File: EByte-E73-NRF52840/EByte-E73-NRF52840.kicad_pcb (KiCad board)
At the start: 2 copper layers, 19.1 x 52.1 mm, 32 parts, among them J1 USB_B_Micro, J2 SWD Header, J3 Conn_01x02, Q1 TP0610T, SW1 DFU, SW2 FRST, U1 ProMicro, U2 E73-2G4M08S1C, U3 AP2112K-3.3, U4 TP4054ST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

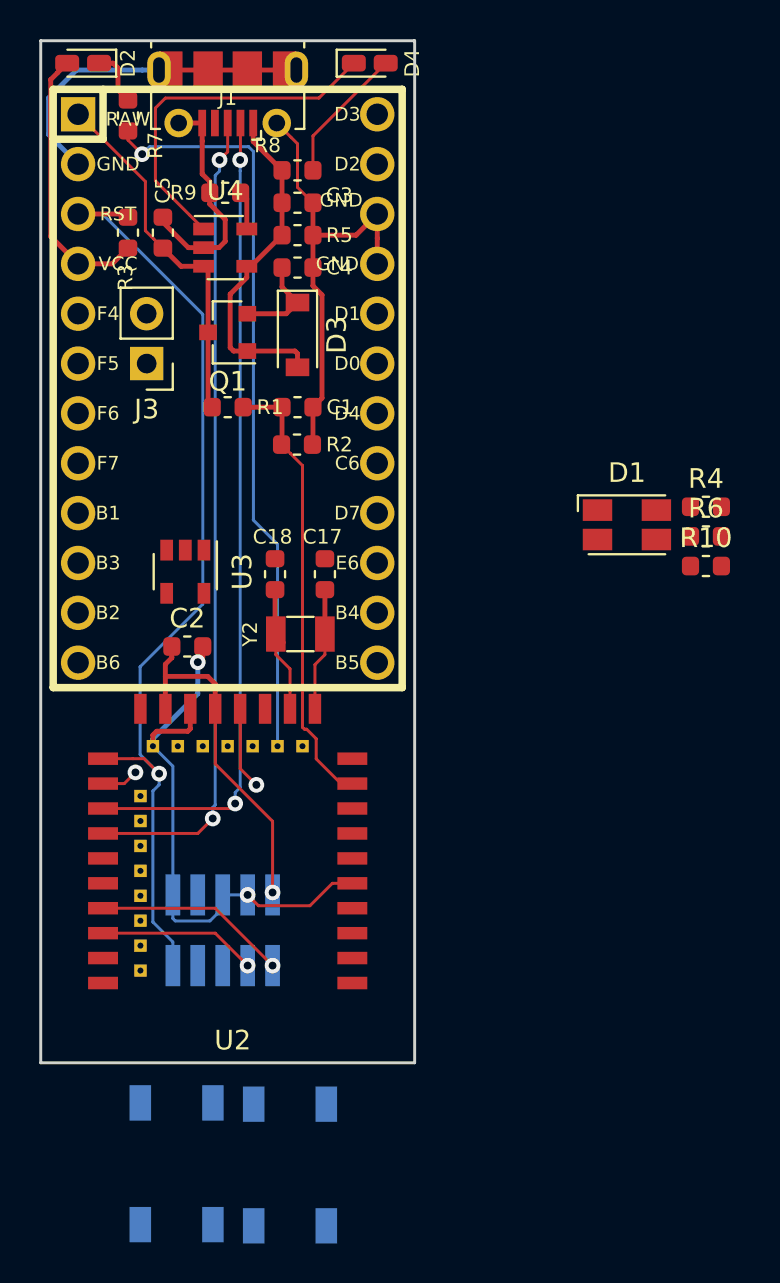
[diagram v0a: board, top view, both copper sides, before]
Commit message: Moved components into PCB area and applied auto router for traces
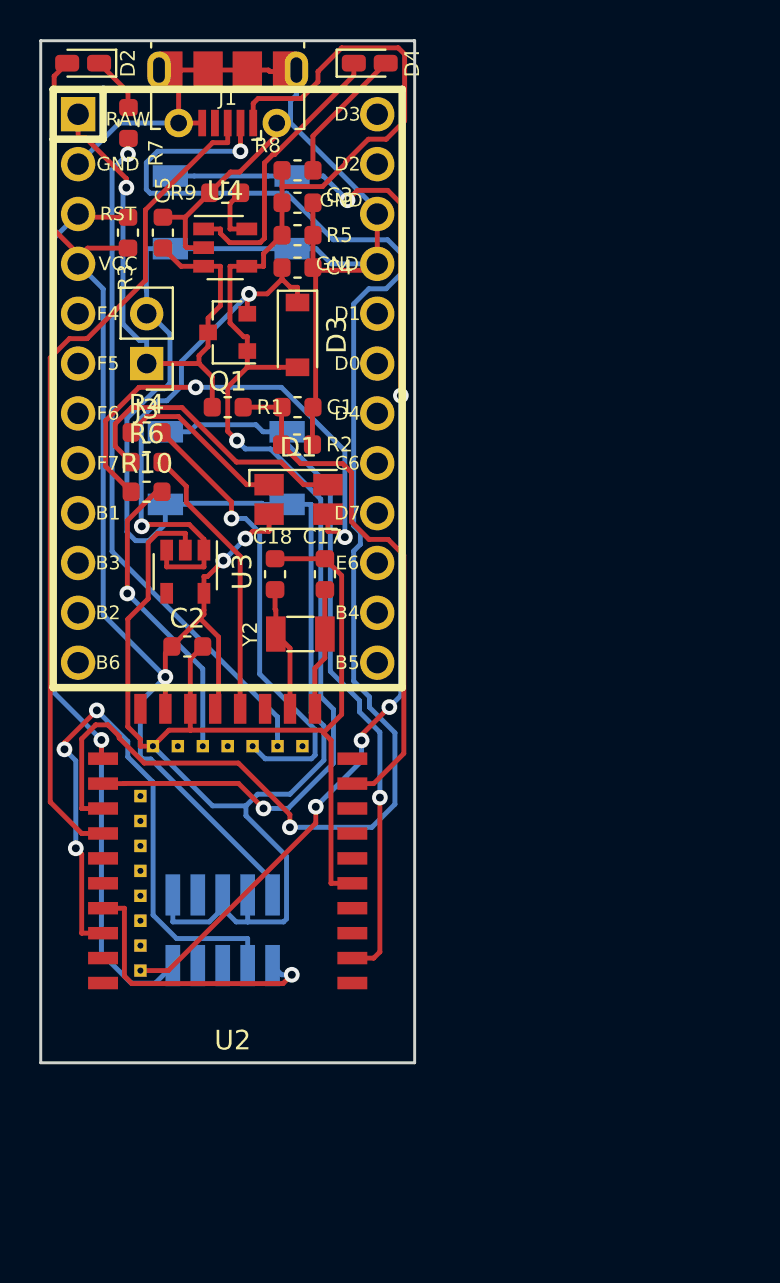
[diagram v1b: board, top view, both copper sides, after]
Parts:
- moved SW1 48.6 mm to (136.7, 83.7), turned to 0 degrees
- moved SW2 35.7 mm to (136.4, 96.7), turned to 0 degrees
- moved R10 28.7 mm to (132.4, 97.9)
- moved R4 28.7 mm to (132.4, 94.9)
- moved R6 28.7 mm to (132.4, 96.4)
- moved D1 16.8 mm to (140.1, 98.3)
- moved R7 0.38 mm to (131.5, 79.1)
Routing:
- net GND: track 84.1 -> 185.2 mm, vias 2 -> 0
- net /SW1: track 0.00 -> 58.1 mm, vias 0 -> 5
- net /VBus: track 19.4 -> 73.3 mm, vias 1 -> 2
- net /P1.10: track 0.00 -> 36.7 mm, vias 0 -> 1
- net /D-: track 41.6 -> 76.9 mm
- net VDD: track 34.4 -> 69.5 mm, vias 1 -> 3
- net Net-(D1-Pad3): track 0.00 -> 24.6 mm, vias 0 -> 2
- net /SWDCLK: track 8.05 -> 31.8 mm, vias 1 -> 3
- net /LED2R: track 0.00 -> 23.6 mm, vias 0 -> 1
- net Net-(C4-Pad1): track 5.10 -> 27.4 mm, vias 0 -> 2
- net /LED2B: track 0.00 -> 15.5 mm, vias 0 -> 1
- net Net-(D1-Pad2): track 0.00 -> 15.1 mm
- net /VBatt: track 19.3 -> 29.4 mm, vias 0 -> 1
- net /LED2G: track 4.22 -> 14.2 mm, vias 1 -> 0
- net Net-(D1-Pad1): track 0.00 -> 8.80 mm
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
